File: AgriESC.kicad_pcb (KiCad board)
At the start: 2 copper layers, 94.5 x 53.5 mm, 309 parts, among them J1 SUPPLY, J10 GPIO, J11 USB_OTG, J12 HALL_ENC, J2 PH_A, J3 PH_B, J4 PH_C, J6 COMM, J7 SERVO, J8 CAN, J9 SWD, SW1 SW_SPDT, U1 FDMS7698, U10 STM32F405RGT6, U11 DRV8303, U12 TJA1051TK-3, U13 LMR16006YQ, U14 MCP1700-3302E_SOT23, U15 MCP1700-3302E_SOT23, U2 FDMS7698, U3 FDMS7698, U4 FDMS7698, U5 FDMS7698, U6 FDMS7698, U7 MAX9920, U8 MAX9920, U9 MAX9920, Y1 8M Resonator

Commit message: Working through the routing
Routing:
- net +5V: track 30.7 -> 120.7 mm, vias 0 -> 5
- net VCC: track 36.3 -> 107.7 mm, vias 0 -> 8
- net SL_A: track 307.6 -> 358.6 mm, vias 16 -> 21
- net SWDIO: track 0.00 -> 30.8 mm, vias 0 -> 2
- net USB_DP: track 0.00 -> 30.4 mm, vias 0 -> 2
- net USB_DM: track 0.00 -> 29.8 mm, vias 0 -> 2
- net EN_GATE: track 5.13 -> 31.7 mm, vias 0 -> 2
- net PB12: track 0.00 -> 26.5 mm, vias 0 -> 1
- net HALL_1: track 9.42 -> 30.0 mm, vias 0 -> 2
- net HALL_3: track 9.23 -> 28.8 mm, vias 0 -> 2
- net CANL: track 2.26 -> 21.7 mm, vias 0 -> 3
- net CANH: track 2.94 -> 22.3 mm, vias 0 -> 3
- net FAULT: track 9.88 -> 29.2 mm, vias 0 -> 2
- net HALL_2: track 9.28 -> 27.7 mm, vias 0 -> 2
- net NRST: track 5.83 -> 23.5 mm, vias 0 -> 2
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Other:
- board size 94.5 x 53.5 mm -> 94.6 x 69.2 mm

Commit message: PCB routing
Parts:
- moved D3 33.1 mm to (77.7, 15.7), turned to 0 degrees
- moved D2 32.1 mm to (73.7, 15.7), turned to 180 degrees
- moved R24 30.8 mm to (77.7, 14.2), turned to 180 degrees
- moved R23 25.9 mm to (74.4, 18.3), turned to 90 degrees
- moved D1 11.2 mm to (69.1, 42.0), turned to 90 degrees
- moved R22 9.70 mm to (69.1, 45.8), turned to 90 degrees
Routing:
- net SL_A: track 358.6 -> 449.5 mm, vias 21 -> 32
- net CAN_TX: track 0.00 -> 48.2 mm, vias 0 -> 4
- net CAN_RX: track 0.00 -> 46.7 mm, vias 0 -> 4
- net RX_SDA_NSS: track 0.00 -> 40.4 mm, vias 0 -> 4
- net TX_SCL_MOSI: track 0.00 -> 37.6 mm, vias 0 -> 3
- net SERVO: track 0.00 -> 32.8 mm, vias 0 -> 3
- net VCC: track 107.7 -> 139.2 mm, vias 8 -> 10
- net SWCLK: track 0.00 -> 28.1 mm, vias 0 -> 3
- net SCK_ADC_EXT: track 0.00 -> 27.2 mm, vias 0 -> 3
- net MISO_ADC_EXT2: track 0.00 -> 22.4 mm, vias 0 -> 3
- net Net-(D2-Pad2): track 0.00 -> 19.9 mm, vias 0 -> 2
- net ADC_15: track 0.00 -> 17.8 mm, vias 0 -> 2
- net TEMP_MOTOR: track 10.6 -> 27.8 mm, vias 0 -> 2
- net Net-(D3-Pad2): track 0.00 -> 15.4 mm, vias 0 -> 2
- net HALL_3: track 28.8 -> 31.8 mm
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
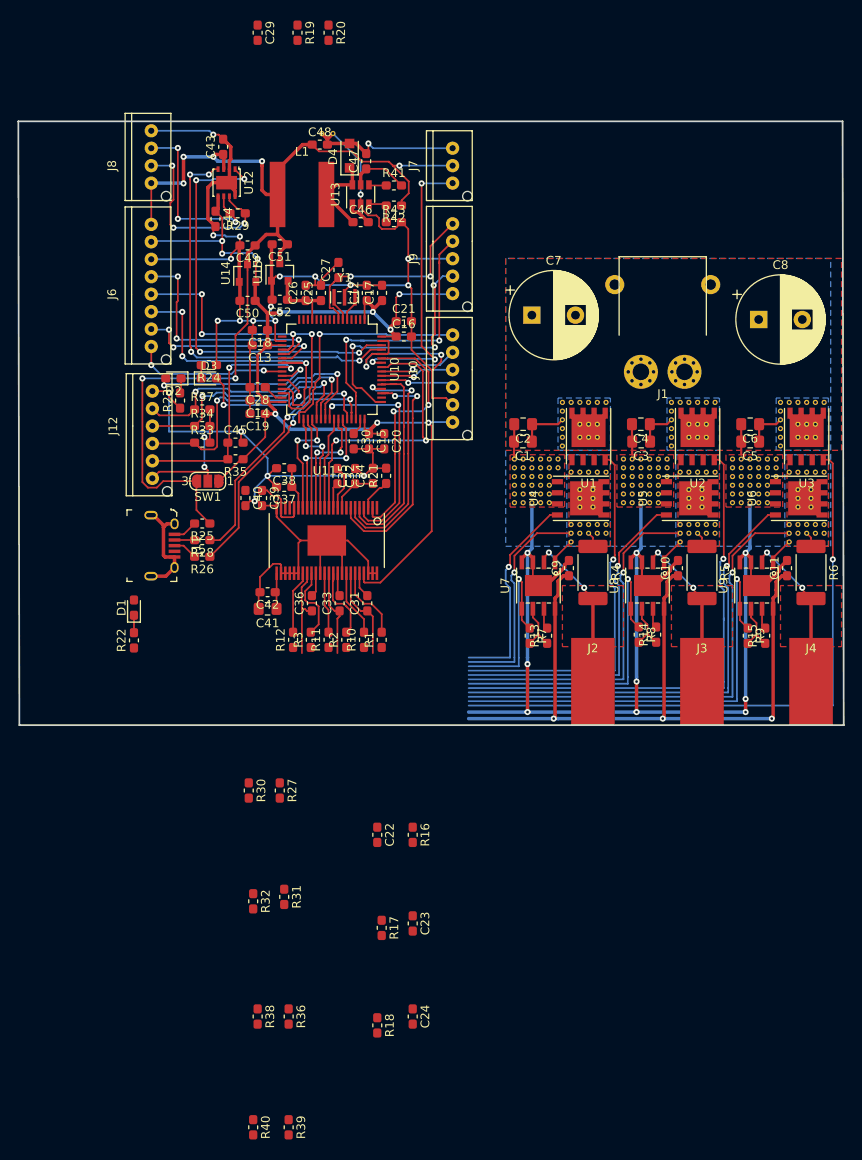
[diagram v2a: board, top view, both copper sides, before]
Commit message: More routing, and an adjustment to the USB connector shield/ground
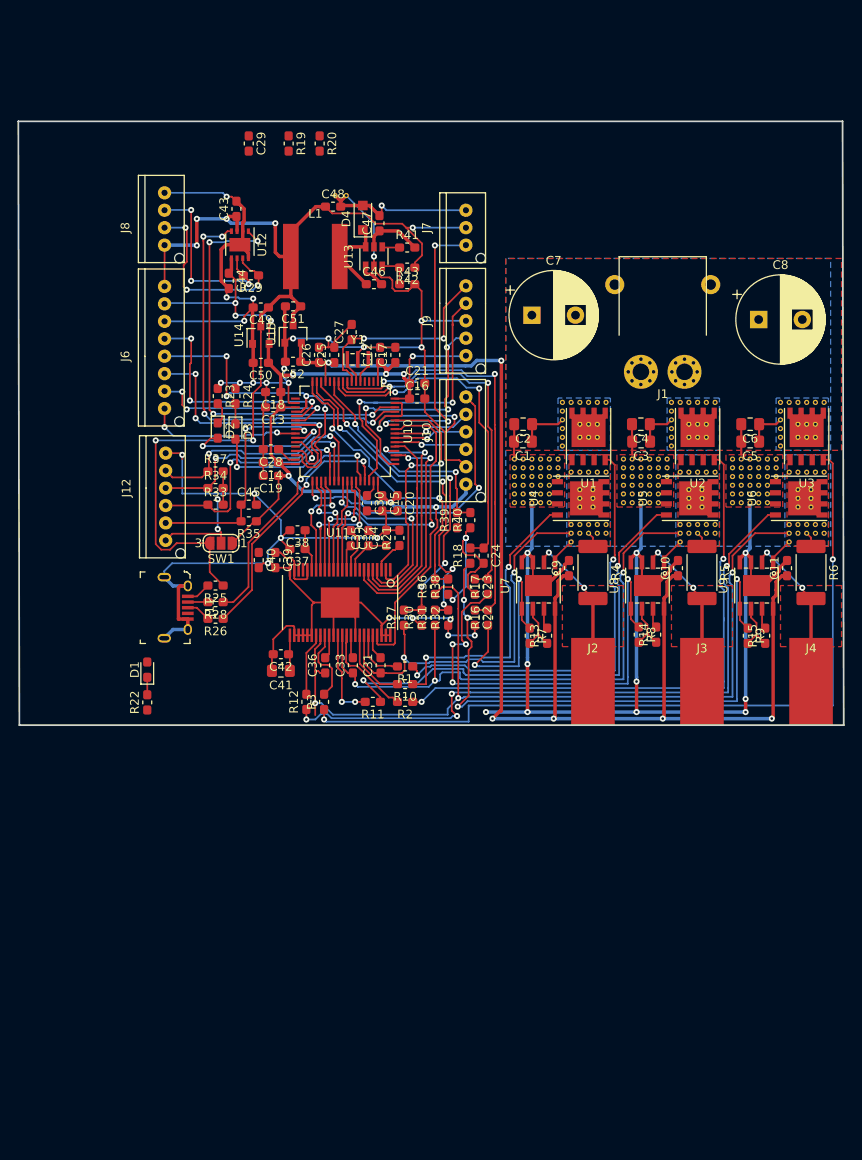
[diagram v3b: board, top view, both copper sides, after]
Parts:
- added REF**: VIA-0.6mm, AgriESC:VIA-0.6mm, F.Cu at (117.8, 27.0)
- U12: footprint Package_DFN_QFN:DFN-8-1EP_3x3mm_P0.65mm_EP1.55x2.4mm -> Housings_DFN_QFN:DFN-8-1EP_3x3mm_Pitch0.65mm
- moved R40 73.9 mm to (107.7, 32.0), turned to 90 degrees
- moved R39 72.2 mm to (106.2, 32.0), turned to 90 degrees
- moved R18 54.9 mm to (107.7, 36.1), turned to 90 degrees
- moved R38 53.9 mm to (105.2, 39.6), turned to 90 degrees
- moved C24 53.5 mm to (109.2, 36.1)
- moved R36 52.0 mm to (103.6, 39.6), turned to 90 degrees
- moved R17 41.0 mm to (109.7, 39.6), turned to 90 degrees
- moved R32 39.5 mm to (105.2, 43.2), turned to 90 degrees
- moved C23 39.3 mm to (108.2, 39.6)
- moved R31 36.4 mm to (103.6, 43.2), turned to 90 degrees
- moved R30 28.0 mm to (102.1, 43.2), turned to 90 degrees
- moved C22 27.3 mm to (108.2, 43.2)
- moved R16 26.3 mm to (109.7, 43.2), turned to 90 degrees
- moved R27 24.4 mm to (100.1, 43.2), turned to 90 degrees
- moved C29 12.7 mm to (82.3, -11.2)
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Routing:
- net VAA: track 97.2 -> 156.2 mm, vias 3 -> 6
- net CURRENT_1: track 0.00 -> 48.4 mm, vias 0 -> 2
- net SL_A: track 449.5 -> 494.1 mm, vias 32 -> 42
- net CURRENT_2: track 0.00 -> 43.2 mm, vias 0 -> 2
- net SENS_B: track 0.00 -> 40.1 mm, vias 0 -> 4
- net SENS_A: track 0.00 -> 39.5 mm, vias 0 -> 4
- net CURRENT_3: track 0.00 -> 39.0 mm, vias 0 -> 2
- net SH_C: track 69.8 -> 104.5 mm, vias 1 -> 3
- net SENS_C: track 0.00 -> 34.6 mm, vias 0 -> 2
- net SENS_SUPPLY: track 0.00 -> 26.1 mm, vias 0 -> 2
- net Net-(R12-Pad1): track 53.2 -> 77.4 mm, vias 1 -> 4
- net Net-(R3-Pad1): track 70.8 -> 90.4 mm, vias 1 -> 2
- net C_C: track 50.9 -> 70.2 mm, vias 1 -> 4
- net SH_B: track 54.9 -> 72.6 mm, vias 1 -> 3
- net Net-(R11-Pad1): track 38.9 -> 55.6 mm, vias 1 -> 2
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
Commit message: Routing
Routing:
- net SL_A: track 494.1 -> 516.8 mm, vias 42 -> 43
- net Net-(C39-Pad1): track 7.09 -> 9.00 mm
- net Net-(R3-Pad1): track 90.4 -> 89.8 mm
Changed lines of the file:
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@@
     (thickness 1.6)
     (drawings 4)
-    (tracks 1693)
+    (tracks 1713)
     (zones 0)
     (modules 310)
@@
   (segment (start 112.725 22.975) (end 112.7 23) (width 0.25) (layer F.Cu) (net 1) (status 30))
   (segment (start 112.725 21) (end 112.725 22.975) (width 0.25) (layer F.Cu) (net 1) (status 30))
-  (segment (start 112.95 24.55) (end 112.5 25) (width 0.25) (layer F.Cu) (net 1) (status 20))
   (segment (start 112.7 23) (end 112.7 24.55) (width 0.25) (layer F.Cu) (net 1) (status 10))
   (segment (start 138.75 21) (end 138.75 23) (width 0.25) (layer F.Cu) (net 1) (status 30))
-  (segment (start 139.25 24.5) (end 138.75 25) (width 0.25) (layer F.Cu) (net 1) (status 20))
   (segment (start 138.75 23) (end 138.75 24.5) (width 0.25) (layer F.Cu) (net 1) (status 10))
   (segment (start 126.225 22.975) (end 126.25 23) (width 0.25) (layer F.Cu) (net 1) (status 30))
   (segment (start 126.225 21) (end 126.225 22.975) (width 0.25) (layer F.Cu) (net 1) (status 30))
-  (segment (start 126.75 24.5) (end 126.25 25) (width 0.25) (layer F.Cu) (net 1) (status 20))
   (segment (start 126.25 23) (end 126.25 24.5) (width 0.25) (layer F.Cu) (net 1) (status 10))
   (segment (start 127.365 38.865) (end 128 39.5) (width 0.25) (layer F.Cu) (net 1) (status 30))
@@
   (segment (start 108.29501 36.01801) (end 107.235854 36.01801) (width 0.2) (layer F.Cu) (net 1))
   (segment (start 109.22 36.943) (end 108.29501 36.01801) (width 0.2) (layer F.Cu) (net 1))
+  (segment (start 105.423537 41.388463) (end 105.664 41.148) (width 0.2) (layer B.Cu) (net 1))
+  (segment (start 105.423537 43.38) (end 105.423537 41.388463) (width 0.2) (layer B.Cu) (net 1))
+  (segment (start 112.75 24.575736) (end 112.75 25) (width 0.25) (layer F.Cu) (net 1))
+  (segment (start 112.724264 24.55) (end 112.75 24.575736) (width 0.25) (layer F.Cu) (net 1))
+  (segment (start 112.7 24.55) (end 112.724264 24.55) (width 0.25) (layer F.Cu) (net 1))
+  (segment (start 126.25 24.575736) (end 126.25 24.5) (width 0.2) (layer F.Cu) (net 1))
+  (segment (start 126.25 25) (end 126.25 24.575736) (width 0.2) (layer F.Cu) (net 1))
+  (segment (start 138.75 25) (end 138.75 24.5) (width 0.2) (layer F.Cu) (net 1))
+  (segment (start 82.931 27.954) (end 83.961 26.924) (width 0.2) (layer F.Cu) (net 1))
+  (segment (start 82.931 28.956) (end 82.931 27.954) (width 0.2) (layer F.Cu) (net 1))
+  (via (at 91.44 17.13) (size 0.7) (drill 0.3) (layers F.Cu B.Cu) (net 1))
+  (segment (start 91.598 16.972) (end 91.44 17.13) (width 0.2) (layer F.Cu) (net 1))
+  (segment (start 91.598 16.116) (end 91.598 16.972) (width 0.2) (layer F.Cu) (net 1))
+  (segment (start 90.566 16.256) (end 86.868 16.256) (width 0.2) (layer B.Cu) (net 1))
+  (segment (start 91.44 17.13) (end 90.566 16.256) (width 0.2) (layer B.Cu) (net 1))
+  (segment (start 79.883 -5.207) (end 79.756 -5.08) (width 0.4) (layer B.Cu) (net 1))
+  (segment (start 92.202 -5.207) (end 79.883 -5.207) (width 0.4) (layer B.Cu) (net 1))
   (segment (start 114.775 22.975) (end 114.75 23) (width 0.25) (layer F.Cu) (net 2) (status 30))
   (segment (start 114.775 21) (end 114.775 22.975) (width 0.25) (layer F.Cu) (net 2) (status 30))
@@
   (segment (start 87.514 38.671) (end 87.514 37.696) (width 0.2) (layer F.Cu) (net 22) (status 20))
   (segment (start 87.614001 38.771001) (end 87.514 38.671) (width 0.2) (layer F.Cu) (net 22))
+  (segment (start 85.344 35.701) (end 83.439 35.701) (width 0.2) (layer F.Cu) (net 22))
   (segment (start 90.462 -3.937) (end 91.087 -3.937) (width 0.4) (layer F.Cu) (net 23) (status 20))
   (segment (start 89.987 -3.937) (end 90.462 -3.937) (width 0.4) (layer F.Cu) (net 23))
@@
   (segment (start 149.25 25.5) (end 148.826 25.076) (width 0.2) (layer F.Cu) (net 62))
   (segment (start 149.25 36.5) (end 149.25 25.5) (width 0.2) (layer F.Cu) (net 62))
-  (segment (start 149.25 36.5) (end 149.25 53.25) (width 0.2) (layer B.Cu) (net 62))
-  (segment (start 149.25 53.25) (end 107.5 53.25) (width 0.2) (layer B.Cu) (net 62))
-  (segment (start 107.5 53.25) (end 107.5 55.09999) (width 0.2) (layer B.Cu) (net 62))
   (via (at 90.932 54.85) (size 0.7) (drill 0.3) (layers F.Cu B.Cu) (net 62))
-  (segment (start 91.18199 55.09999) (end 90.932 54.85) (width 0.2) (layer B.Cu) (net 62))
-  (segment (start 107.5 55.09999) (end 91.18199 55.09999) (width 0.2) (layer B.Cu) (net 62))
   (segment (start 90.932 54.85) (end 90.932 53.707) (width 0.2) (layer F.Cu) (net 62))
+  (segment (start 91.18199 55.09999) (end 90.932 54.85) (width 0.2) (layer B.Cu) (net 62))
+  (segment (start 107.5 54.083992) (end 106.484002 55.09999) (width 0.2) (layer B.Cu) (net 62))
+  (segment (start 106.484002 55.09999) (end 91.18199 55.09999) (width 0.2) (layer B.Cu) (net 62))
+  (segment (start 107.5 53.25) (end 107.5 54.083992) (width 0.2) (layer B.Cu) (net 62))
+  (segment (start 149.25 53.25) (end 107.5 53.25) (width 0.2) (layer B.Cu) (net 62))
+  (segment (start 149.25 36.5) (end 149.25 53.25) (width 0.2) (layer B.Cu) (net 62))
   (segment (start 114.5 46.125) (end 115.5 45.125) (width 0.2) (layer F.Cu) (net 63) (status 10))
   (segment (start 115.5 45.125) (end 116.5 46.125) (width 0.2) (layer F.Cu) (net 63) (status 20))
@@
   (segment (start 88.914119 27.954119) (end 88.914119 27.275881) (width 0.2) (layer B.Cu) (net 79))
   (segment (start 90.932 25.258) (end 93.228258 25.258) (width 0.2) (layer B.Cu) (net 79))
-  (segment (start 90.598 16.724021) (end 93.157365 19.283386) (width 0.2) (layer F.Cu) (net 80))
-  (segment (start 90.598 16.116) (end 90.598 16.724021) (width 0.2) (layer F.Cu) (net 80))
   (via (at 93.532791 20.97) (size 0.7) (drill 0.3) (layers F.Cu B.Cu) (net 80))
-  (segment (start 93.157365 20.594574) (end 93.532791 20.97) (width 0.2) (layer F.Cu) (net 80))
-  (segment (start 93.157365 19.283386) (end 93.157365 20.594574) (width 0.2) (layer F.Cu) (net 80))
   (segment (start 93.532791 20.97) (end 97.028 24.465209) (width 0.2) (layer B.Cu) (net 80))
   (segment (start 97.028 24.465209) (end 99.486791 26.924) (width 0.2) (layer B.Cu) (net 80))
@@
   (segment (start 102.108 39.624) (end 102.108 41.656) (width 0.2) (layer F.Cu) (net 80))
   (segment (start 102.108 41.656) (end 102.108 42.305) (width 0.2) (layer F.Cu) (net 80))
+  (segment (start 91.043696 17.78) (end 90.598 17.334304) (width 0.2) (layer F.Cu) (net 80))
+  (segment (start 91.653979 17.78) (end 91.043696 17.78) (width 0.2) (layer F.Cu) (net 80))
+  (segment (start 90.598 17.334304) (end 90.598 16.116) (width 0.2) (layer F.Cu) (net 80))
+  (segment (start 93.532791 20.97) (end 93.157365 20.594574) (width 0.2) (layer F.Cu) (net 80))
+  (segment (start 93.157365 20.594574) (end 93.157365 19.283386) (width 0.2) (layer F.Cu) (net 80))
+  (segment (start 93.157365 19.283386) (end 91.653979 17.78) (width 0.2) (layer F.Cu) (net 80))
   (segment (start 95.098 27.516) (end 95.098 26.816) (width 0.2) (layer F.Cu) (net 81) (status 10))
   (via (at 94.74855 24.608) (size 0.7) (drill 0.3) (layers F.Cu B.Cu) (net 81))
@@
   (segment (start 96.098001 25.821999) (end 99.740002 29.464) (width 0.2) (layer B.Cu) (net 83))
   (segment (start 99.740002 29.464) (end 104.14 29.464) (width 0.2) (layer B.Cu) (net 83))
-  (segment (start 94.488 20.048323) (end 94.488 20.977906) (width 0.2) (layer F.Cu) (net 84))
-  (segment (start 92.098 17.658323) (end 94.488 20.048323) (width 0.2) (layer F.Cu) (net 84))
   (via (at 94.488 20.977906) (size 0.7) (drill 0.3) (layers F.Cu B.Cu) (net 84))
-  (segment (start 92.098 16.116) (end 92.098 17.658323) (width 0.2) (layer F.Cu) (net 84))
   (segment (start 94.837999 21.70951) (end 97.536 24.407511) (width 0.2) (layer B.Cu) (net 84))
   (segment (start 94.837999 21.327905) (end 94.837999 21.70951) (width 0.2) (layer B.Cu) (net 84))
@@
   (segment (start 106.172 28.448) (end 106.172 31.129) (width 0.2) (layer F.Cu) (net 84))
   (segment (start 106.029469 28.305469) (end 106.172 28.448) (width 0.2) (layer F.Cu) (net 84))
+  (segment (start 94.488 20.048323) (end 94.488 20.977906) (width 0.2) (layer F.Cu) (net 84))
+  (segment (start 92.098 16.116) (end 92.098001 17.013097) (width 0.2) (layer F.Cu) (net 84))
+  (segment (start 92.964 17.879096) (end 92.964 18.524323) (width 0.2) (layer F.Cu) (net 84))
+  (segment (start 92.098001 17.013097) (end 92.964 17.879096) (width 0.2) (layer F.Cu) (net 84))
+  (segment (start 92.964 18.524323) (end 94.488 20.048323) (width 0.2) (layer F.Cu) (net 84))
   (segment (start 97.667 0.748) (end 97.597 0.678) (width 0.2) (layer F.Cu) (net 85) (status 30))
   (segment (start 99.582 0.748) (end 97.667 0.748) (width 0.2) (layer F.Cu) (net 85) (status 30))

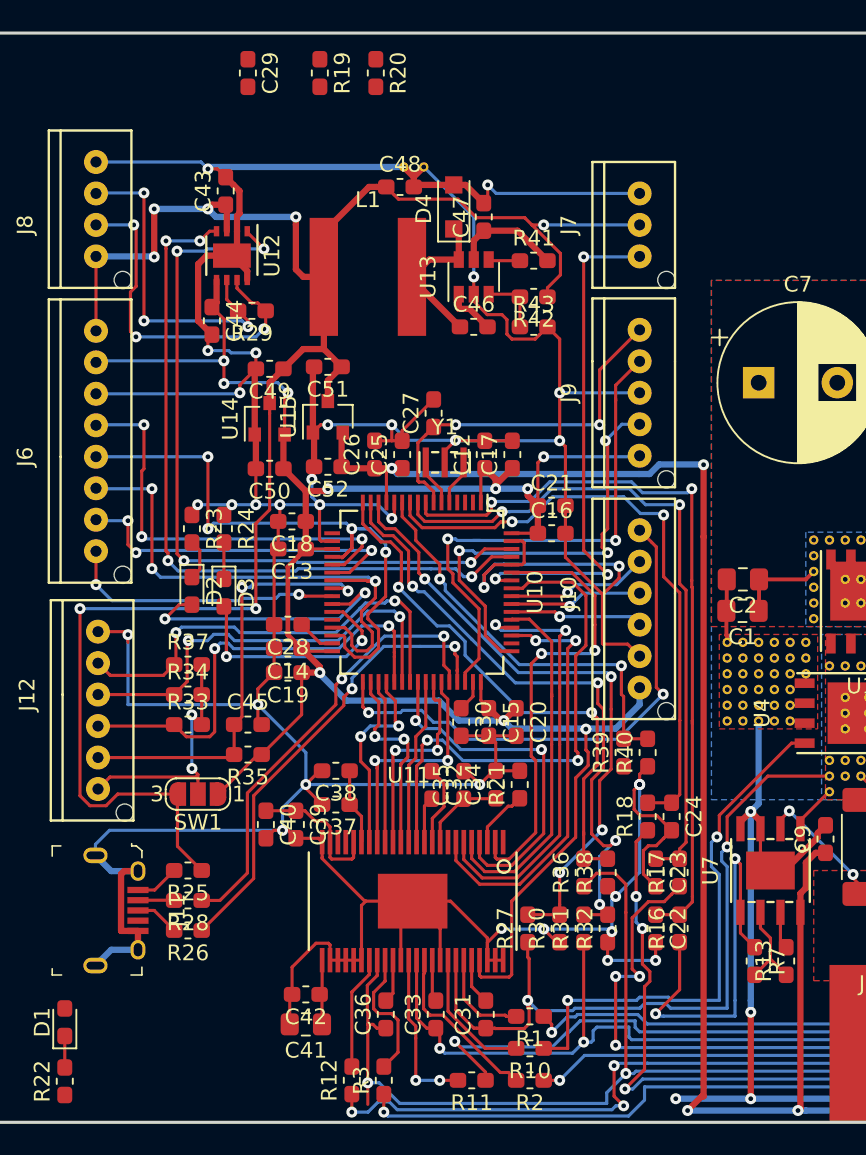
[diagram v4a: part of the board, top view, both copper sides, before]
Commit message: Routed thermistor
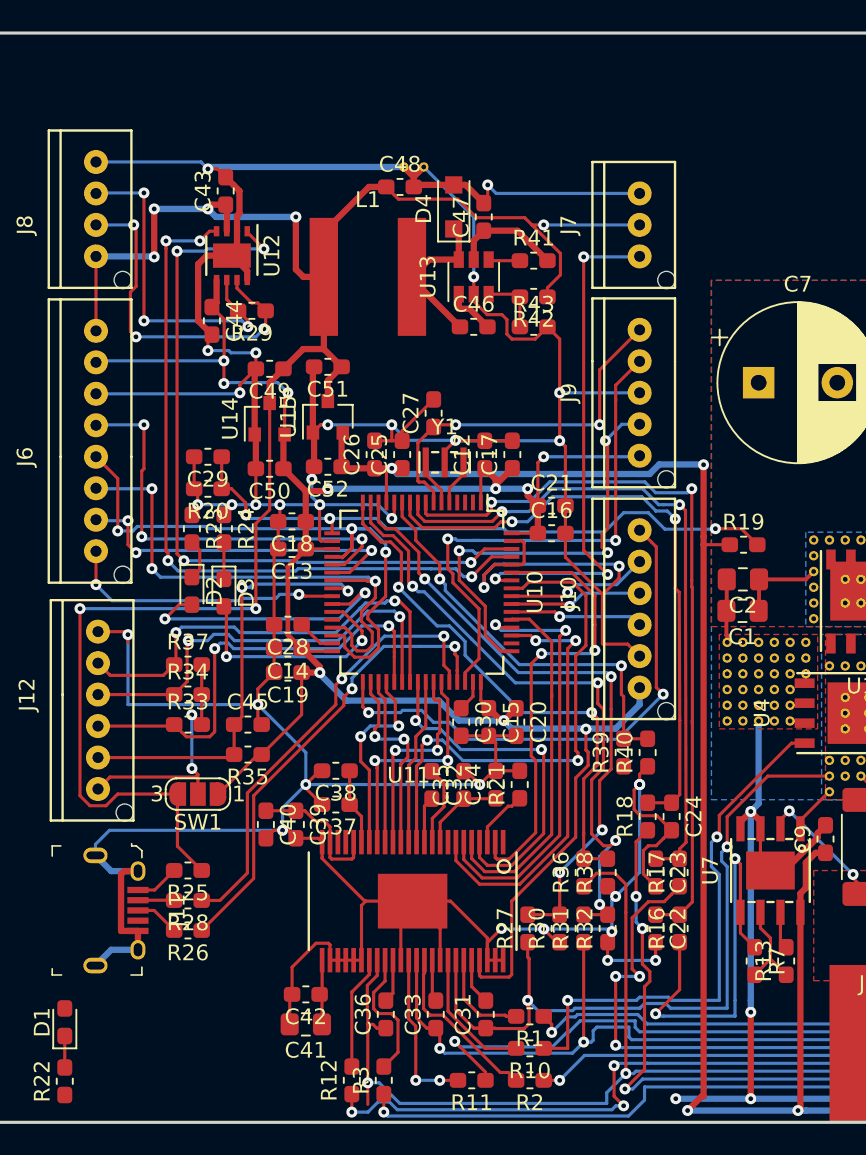
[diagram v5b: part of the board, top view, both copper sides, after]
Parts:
- moved R19 40.3 mm to (113.8, 18.8), turned to 0 degrees
- moved R20 28.5 mm to (79.8, 15.2), turned to 180 degrees
- moved C29 24.5 mm to (79.8, 13.2), turned to 180 degrees
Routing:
- net Net-(C29-Pad1): track 0.00 -> 40.0 mm, vias 0 -> 3
- net SL_A: track 516.8 -> 520.0 mm
- net VAA: track 156.2 -> 157.9 mm
- net RX_SDA_NSS: track 40.3 -> 39.5 mm, vias 4 -> 3
